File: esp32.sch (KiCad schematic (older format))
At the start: 35 parts, among them J10 Conn_01x01, J11 Conn_01x04, J12 Conn_01x01, J13 Conn_01x01, J14 Conn_01x01, J15 Conn_01x01, J16 Conn_01x01, J17 Conn_01x01, J18 Conn_01x02, J19 Conn_01x01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

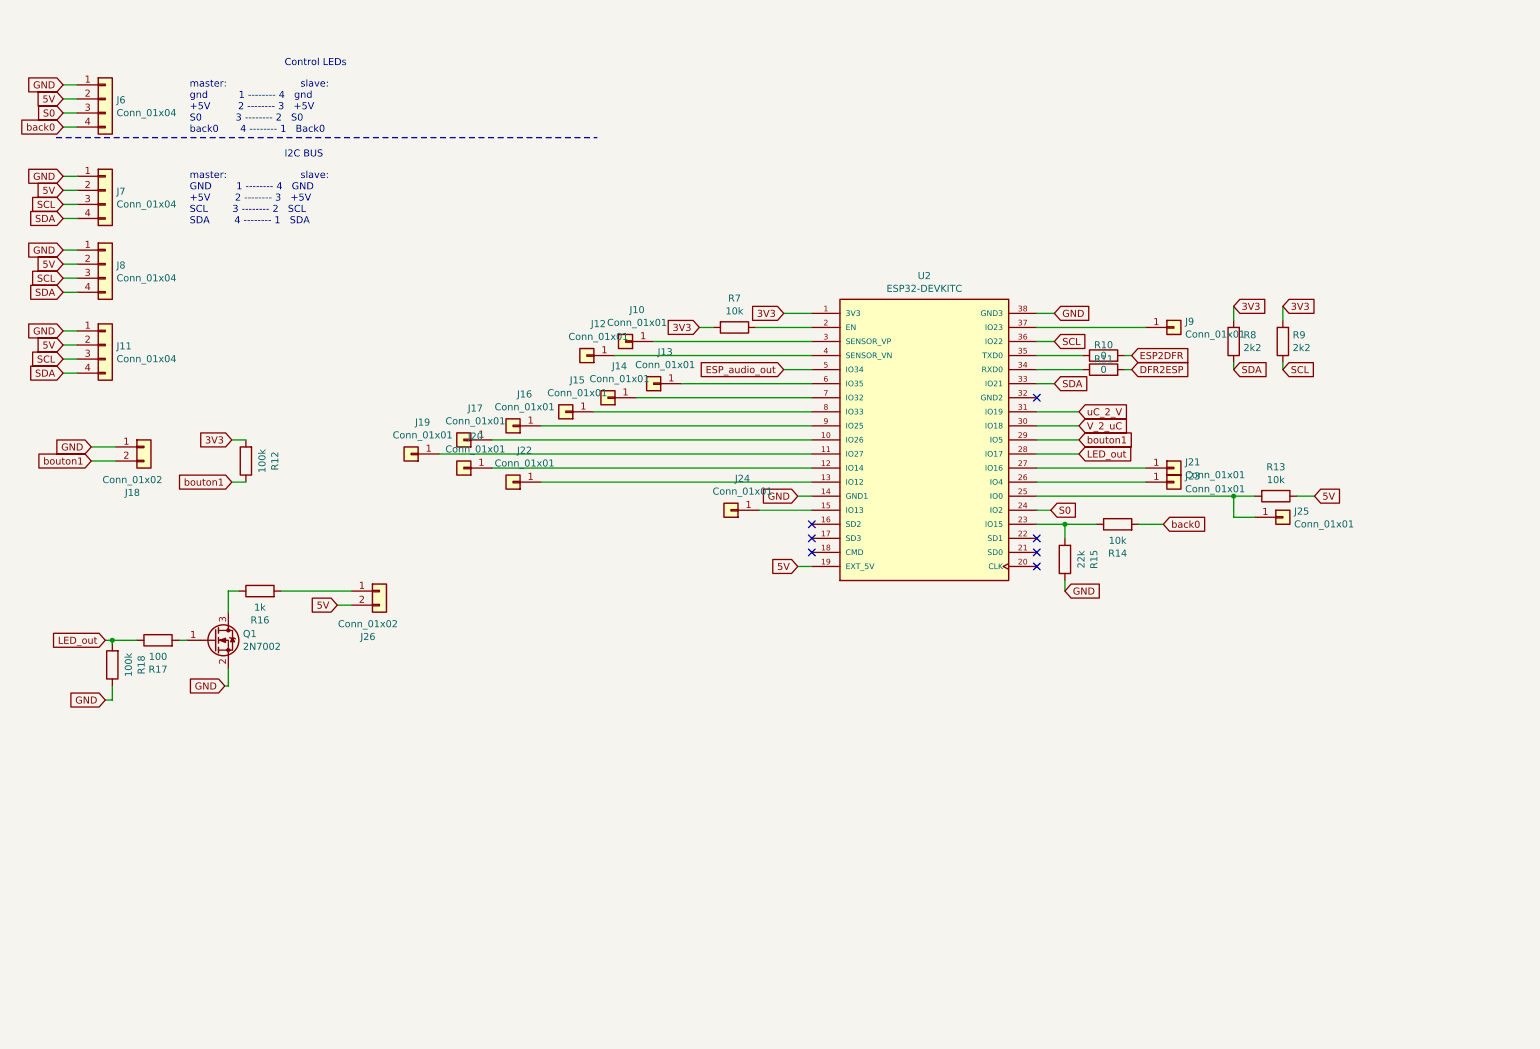
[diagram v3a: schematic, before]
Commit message: simplifying + proper pins for uart + sd card host implemented
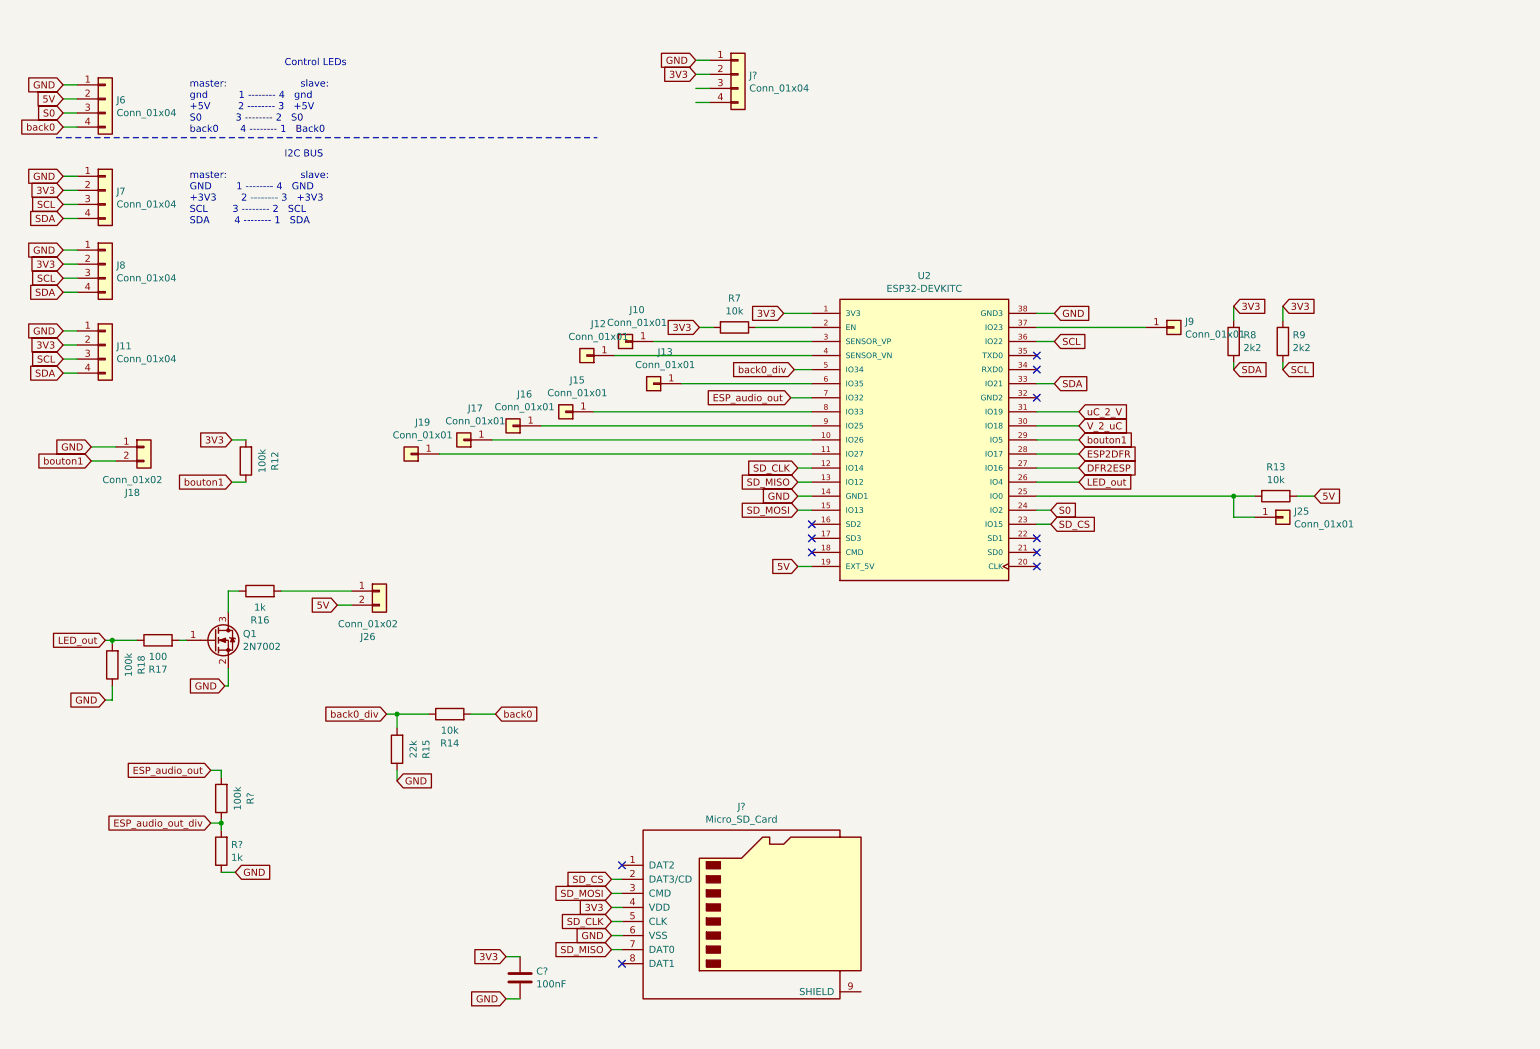
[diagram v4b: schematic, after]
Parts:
- removed J14, J20, J21, J22, J23, J24: Conn_01x01, Connector_PinHeader_2.54mm:PinHeader_1x01_P2.54mm_Vertical, symbol Connector_Generic:Conn_01x01
- removed R10, R11: 0, Resistor_SMD:R_0603_1608Metric_Pad1.05x0.95mm_HandSolder, symbol Device:R
- added C?: 100nF, Capacitor_SMD:C_0603_1608Metric, symbol Device:C
- added J?: Conn_01x04, Connector_JST:JST_XH_B4B-XH-A_1x04_P2.50mm_Vertical, symbol Connector_Generic:Conn_01x04
- added J?: Micro_SD_Card, symbol Connector:Micro_SD_Card
- added R?: 1k, Resistor_SMD:R_0603_1608Metric_Pad1.05x0.95mm_HandSolder, symbol Device:R
- added R?: 100k, Resistor_SMD:R_0603_1608Metric_Pad1.05x0.95mm_HandSolder, symbol Device:R
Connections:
- net 3V3: now also J11.2 (Pin_2), J7.2 (Pin_2), J8.2 (Pin_2), C?.1, J?.2 (Pin_2), J?.4 (VDD)
- net 5V: no longer J11.2 (Pin_2), J7.2 (Pin_2), J8.2 (Pin_2)
- net DFR2ESP: now also U2.27 (IO16)
- net ESP2DFR: now also U2.28 (IO17)
- net ESP_audio_out: now also U2.7 (IO32), R?.2; no longer U2.5 (IO34)
- net GND: now also C?.2, J?.1 (Pin_1), J?.6 (VSS), R?.1
- net LED_out: now also U2.26 (IO4); no longer U2.28 (IO17)
- net SD_CLK: now reaches U2.12 (IO14)
- net SD_CLK: now also J?.5 (CLK)
- net SD_MISO: now reaches U2.13 (IO12)
- net SD_MISO: now also J?.7 (DAT0)
- net SD_MOSI: now reaches U2.15 (IO13)
- net SD_MOSI: now also J?.3 (CMD)
- net back0_div: now reaches R14.1, R15.2
- net back0_div: now also U2.5 (IO34); no longer U2.23 (IO15)
- new net ESP_audio_out_div: R?.1, R?.2
- new net SD_CS: J?.2 (DAT3/CD), U2.23 (IO15)
- no-connect marks 7 -> 11
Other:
- note added: "master: slave:\nGND 1 -------- 4 GND\n+3V3 2 -------- 3 +3V3\nSCL 3 -------- 2 SCL\nSDA 4 -------- 1 SDA"
- note removed: "master: slave:\nGND 1 -------- 4 GND\n+5V 2 -------- 3 +5V\nSCL 3 -------- 2 SCL\nSDA 4 -------- 1 SDA"
- moved on the sheet: R14, R15

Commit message: maj
simplification dfr
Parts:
- removed J16, J17, J19, J9: Conn_01x01, Connector_PinHeader_2.54mm:PinHeader_1x01_P2.54mm_Vertical, symbol Connector_Generic:Conn_01x01
- removed J?: Conn_01x04, Connector_JST:JST_XH_B4B-XH-A_1x04_P2.50mm_Vertical, symbol Connector_Generic:Conn_01x04
- added J14: Conn_01x01, Connector_PinHeader_2.54mm:PinHeader_1x01_P2.54mm_Vertical, symbol Connector_Generic:Conn_01x01
- added J2: Conn_01x06, Connector_PinSocket_2.54mm:PinSocket_1x06_P2.54mm_Vertical, symbol Connector_Generic:Conn_01x06
- added J3: Conn_01x09, Connector_PinSocket_2.54mm:PinSocket_1x09_P2.54mm_Vertical, symbol Connector_Generic:Conn_01x09
- added R11, R19: 10k, Resistor_SMD:R_0603_1608Metric_Pad1.05x0.95mm_HandSolder, symbol Device:R
- added R22, R23, R24, R25, R26, R27, R29, R31, R32, R33, R35, R37, R38, R40, R42, R43: 0, Resistor_SMD:R_0603_1608Metric_Pad1.05x0.95mm_HandSolder, symbol Device:R
- J1: renamed from J?; footprint (none) -> Connector_Card:microSD_HC_Molex_104031-0811
- gave numbers to parts that had none: 3
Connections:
- net ESP2DFR is gone; now on an unnamed net: U2.28 (IO17)
- net V_2_uC is gone; now on an unnamed net: U2.30 (IO18)
- net 3V3: now also R13.1, J2.1 (Pin_1), R11.2, R19.2
- net 5V: now also J3.1 (Pin_1); no longer R13.1
- net ESP_audio_out: now also R22.1; no longer U2.7 (IO32)
- net GND: now also J1.9 (SHIELD), J2.2 (Pin_2), J3.3 (Pin_3), J3.8 (Pin_8), R43.2
- net LED_out: now also R38.1; no longer U2.26 (IO4)
- net SD_CLK: now also R35.2; no longer U2.12 (IO14)
- net SD_CS: now also R11.1, R42.1; no longer U2.23 (IO15)
- net SD_MISO: now also R19.1, R37.2; no longer U2.13 (IO12)
- net SD_MOSI: now also R40.2; no longer U2.15 (IO13)
- net back0_div: now also R24.1; no longer U2.5 (IO34)
- net bouton1: now also R32.1; no longer U2.29 (IO5)
- net at U2.10 (IO26): now also R31.1
- net at U2.11 (IO27): now also R33.1
- net at U2.37 (IO23): now also R22.2
- net at J12.1 (Pin_1): no longer U2.4 (SENSOR_VN)
- net at J13.1 (Pin_1): now also U2.29 (IO5); no longer U2.6 (IO35)
- net at J15.1 (Pin_1): no longer U2.8 (IO33)
- net at U2.9 (IO25): now also R29.1
- net DFR2ESP: no longer names the net of U2.27 (IO16)
- net DFR2ESP: now also R32.2
- net uC_2_V: no longer names the net of U2.31 (IO19)
- net uC_2_V: now also R38.2
- new net: R35.1, U2.12 (IO14)
- new net: R37.1, U2.13 (IO12)
- new net: R40.1, U2.15 (IO13)
- new net: R42.2, U2.23 (IO15)
- new net: R24.2, U2.26 (IO4)
- new net: R23.1, U2.4 (SENSOR_VN)
- new net: J14.1 (Pin_1), U2.5 (IO34)
- new net: R25.1, U2.6 (IO35)
- new net: R26.1, U2.7 (IO32)
- new net: R27.1, U2.8 (IO33)
- new net: J2.6 (Pin_6), R43.1
- new net DAC_Lout: J3.7 (Pin_7)
- new net DAC_Rout: J3.9 (Pin_9)
- new net TILT: R23.2
- new net mic_BCLK: J2.3 (Pin_3), R27.2
- new net mic_DOUT: J2.4 (Pin_4), R25.2
- new net mic_LRCL: J2.5 (Pin_5), R26.2
- new net out_BCLK: J3.6 (Pin_6), R33.2
- new net out_DIN: J3.5 (Pin_5), R31.2
- new net out_WSEL: J3.4 (Pin_4), R29.2
- no-connect marks 11 -> 12
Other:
- note added: "kit adafruit SPH0645LM4H"
- moved on the sheet: C7, J1, J10, J18, J25, J26, Q1, R10, R12, R13, R14, R15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

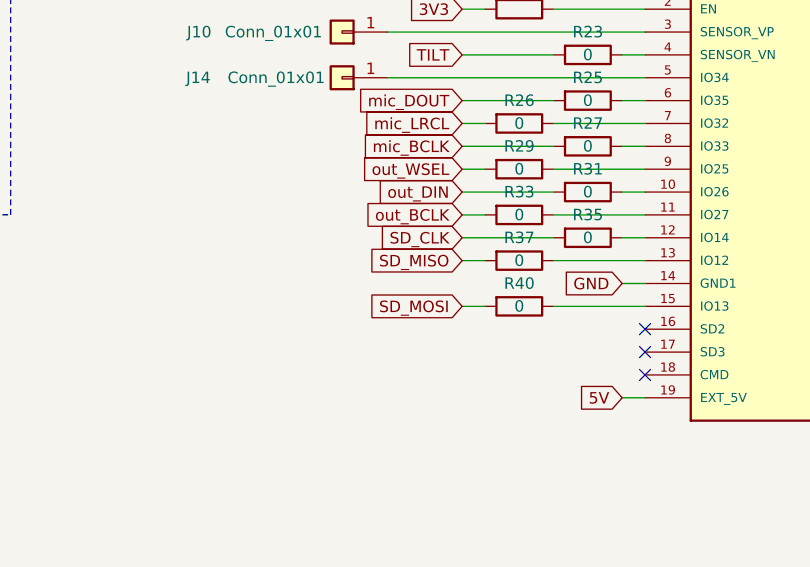
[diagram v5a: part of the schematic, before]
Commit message: inversion miso et mosi sdcard
problème de pull-up au démarrage qui bloque l'esp32. Résolu en permutant les deux fils. schéma et routage corrigés
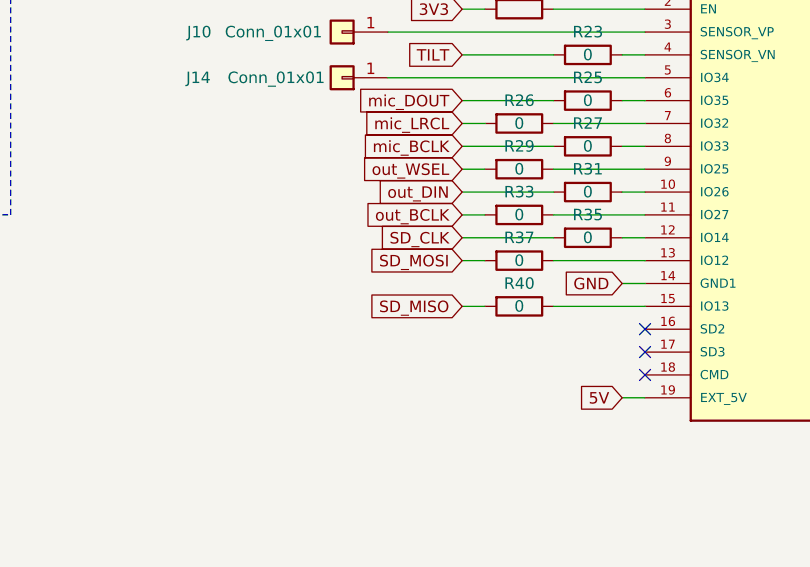
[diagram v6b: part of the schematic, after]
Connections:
- net SD_MISO: now also R40.2; no longer R37.2
- net SD_MOSI: now also R37.2; no longer R40.2
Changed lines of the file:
@@
 Text GLabel 8400 3350 2    50   Input ~ 0
 back0_div
+Text GLabel 5200 3550 0    50   Input ~ 0
+SD_MISO
 Text GLabel 5200 3350 0    50   Input ~ 0
-SD_MISO
-Text GLabel 5200 3550 0    50   Input ~ 0
 SD_MOSI
 Text GLabel 5200 3250 0    50   Input ~ 0

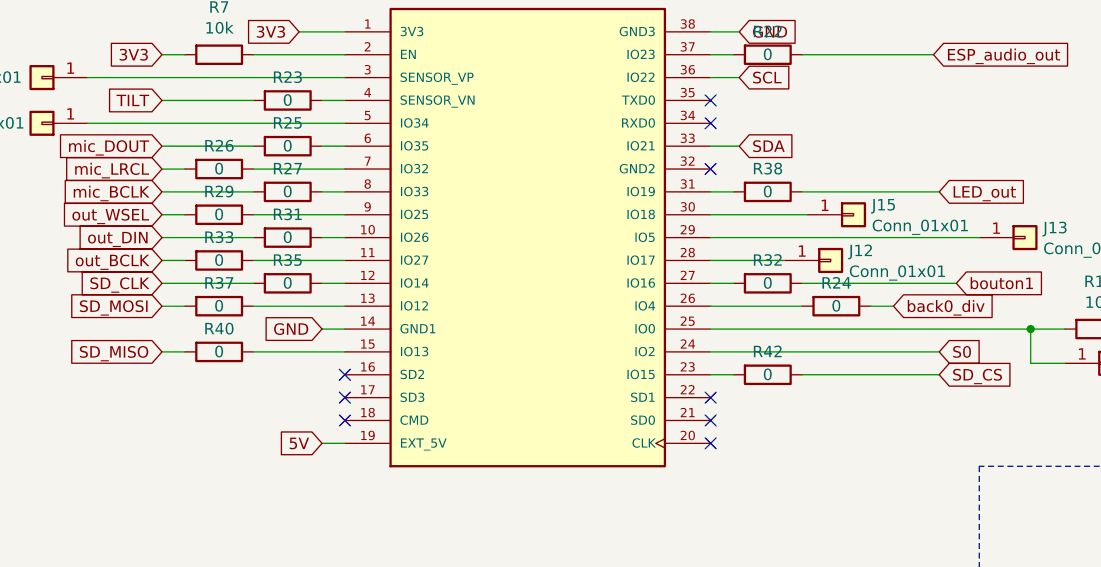
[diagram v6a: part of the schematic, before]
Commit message: simplification
effacé les straps des fonctions sd card et dac audio
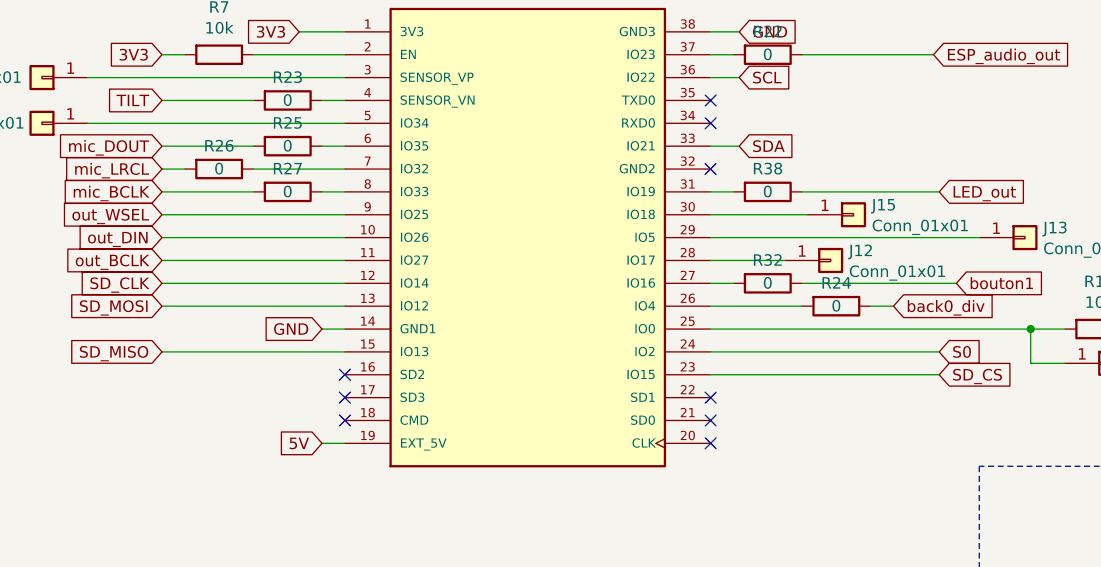
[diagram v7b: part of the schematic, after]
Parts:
- removed R29, R31, R33, R35, R37, R40, R42: 0, Resistor_SMD:R_0603_1608Metric_Pad1.05x0.95mm_HandSolder, symbol Device:R
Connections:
- net SD_CLK: now also U2.12 (IO14)
- net SD_CS: now also U2.23 (IO15)
- net SD_MISO: now also U2.15 (IO13)
- net SD_MOSI: now also U2.13 (IO12)
- net out_BCLK: now also U2.11 (IO27)
- net out_DIN: now also U2.10 (IO26)
- net out_WSEL: now also U2.9 (IO25)
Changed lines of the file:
@@
 Text GLabel 8600 3650 2    50   Input ~ 0
 SD_CS
-Wire Wire Line
-	5900 3250 6000 3250
-Wire Wire Line
-	7600 3650 7700 3650
 $Comp
 L Device:R R19
@@
 	0    1    1    0
 $EndComp
-$Comp
-L Device:R R29
-U 1 1 6039093D
-P 5450 2950
-F 0 "R29" V 5350 2950 50  0000 C CNN
-F 1 "0" V 5450 2950 50  0000 C CNN
-F 2 "Resistor_SMD:R_0603_1608Metric_Pad1.05x0.95mm_HandSolder" V 5380 2950 50  0001 C CNN
-F 3 "~" H 5450 2950 50  0001 C CNN
-	1    5450 2950
-	0    1    1    0
-$EndComp
-$Comp
-L Device:R R31
-U 1 1 60390C94
-P 5750 3050
-F 0 "R31" V 5650 3050 50  0000 C CNN
-F 1 "0" V 5750 3050 50  0000 C CNN
-F 2 "Resistor_SMD:R_0603_1608Metric_Pad1.05x0.95mm_HandSolder" V 5680 3050 50  0001 C CNN
-F 3 "~" H 5750 3050 50  0001 C CNN
-	1    5750 3050
-	0    1    1    0
-$EndComp
-$Comp
-L Device:R R33
-U 1 1 603911D4
-P 5450 3150
-F 0 "R33" V 5350 3150 50  0000 C CNN
-F 1 "0" V 5450 3150 50  0000 C CNN
-F 2 "Resistor_SMD:R_0603_1608Metric_Pad1.05x0.95mm_HandSolder" V 5380 3150 50  0001 C CNN
-F 3 "~" H 5450 3150 50  0001 C CNN
-	1    5450 3150
-	0    1    1    0
-$EndComp
-$Comp
-L Device:R R35
-U 1 1 603915F4
-P 5750 3250
-F 0 "R35" V 5650 3250 50  0000 C CNN
-F 1 "0" V 5750 3250 50  0000 C CNN
-F 2 "Resistor_SMD:R_0603_1608Metric_Pad1.05x0.95mm_HandSolder" V 5680 3250 50  0001 C CNN
-F 3 "~" H 5750 3250 50  0001 C CNN
-	1    5750 3250
-	0    1    1    0
-$EndComp
-$Comp
-L Device:R R37
-U 1 1 60391B58
-P 5450 3350
-F 0 "R37" V 5350 3350 50  0000 C CNN
-F 1 "0" V 5450 3350 50  0000 C CNN
-F 2 "Resistor_SMD:R_0603_1608Metric_Pad1.05x0.95mm_HandSolder" V 5380 3350 50  0001 C CNN
-F 3 "~" H 5450 3350 50  0001 C CNN
-	1    5450 3350
-	0    1    1    0
-$EndComp
-$Comp
-L Device:R R40
-U 1 1 603925BD
-P 5450 3550
-F 0 "R40" V 5350 3550 50  0000 C CNN
-F 1 "0" V 5450 3550 50  0000 C CNN
-F 2 "Resistor_SMD:R_0603_1608Metric_Pad1.05x0.95mm_HandSolder" V 5380 3550 50  0001 C CNN
-F 3 "~" H 5450 3550 50  0001 C CNN
-	1    5450 3550
-	0    1    1    0
-$EndComp
 Wire Wire Line
 	5200 2750 5300 2750
@@
 Wire Wire Line
 	5900 2850 6000 2850
-Wire Wire Line
-	5600 2950 6000 2950
-Wire Wire Line
-	5900 3050 6000 3050
-Wire Wire Line
-	5600 3150 6000 3150
-Wire Wire Line
-	5200 3250 5600 3250
-Wire Wire Line
-	5200 3350 5300 3350
-Wire Wire Line
-	5200 3550 5300 3550
-Wire Wire Line
-	5600 3350 6000 3350
-Wire Wire Line
-	5600 3550 6000 3550
 $Comp
 L Device:R R32
@@
 Wire Wire Line
 	7600 3350 8000 3350
-$Comp
-L Device:R R42
-U 1 1 60405C8C
-P 7850 3650
-F 0 "R42" V 7750 3650 50  0000 C CNN
-F 1 "0" V 7850 3650 50  0000 C CNN
-F 2 "Resistor_SMD:R_0603_1608Metric_Pad1.05x0.95mm_HandSolder" V 7780 3650 50  0001 C CNN
-F 3 "~" H 7850 3650 50  0001 C CNN
-	1    7850 3650
-	0    1    1    0
-$EndComp
-Wire Wire Line
-	8000 3650 8600 3650
 Text GLabel 5200 2750 0    50   Input ~ 0
 mic_LRCL
@@
 Wire Wire Line
 	5200 2850 5600 2850
-Wire Wire Line
-	5200 2950 5300 2950
 Text GLabel 9575 3450 2    50   Input ~ 0
 3V3
@@
 Text GLabel 5200 3150 0    50   Input ~ 0
 out_BCLK
-Wire Wire Line
-	5200 3150 5300 3150
-Wire Wire Line
-	5200 3050 5600 3050
 $Comp
 L Device:R R22
@@
 Wire Wire Line
 	7600 3050 8775 3050
+Wire Wire Line
+	5200 3250 6000 3250
+Wire Wire Line
+	5200 3350 6000 3350
+Wire Wire Line
+	5200 3550 6000 3550
+Wire Wire Line
+	7600 3650 8600 3650
+Wire Wire Line
+	5200 3150 6000 3150
+Wire Wire Line
+	5200 3050 6000 3050
+Wire Wire Line
+	5200 2950 6000 2950
 $EndSCHEMATC
